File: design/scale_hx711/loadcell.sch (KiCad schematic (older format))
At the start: 12 parts

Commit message: Adds new footprints, and BoM.
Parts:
- J3: renamed from J?; footprint (none) -> Connector_JST:JST_EH_B4B-EH-A_1x04_P2.50mm_Vertical
- Q3: renamed from Q?; value BC560 -> BC857; footprint Package_TO_SOT_THT:TO-92_Inline -> Package_TO_SOT_SMD:SOT-23
- R6, R7, R8, R9: renamed from R?; footprint (none) -> Resistor_SMD:R_0603_1608Metric_Pad1.05x0.95mm_HandSolder
- U4: renamed from U?; footprint SO16 -> Package_SO:SOIC-16_3.9x9.9mm_P1.27mm
- gave numbers to parts that had none: 5
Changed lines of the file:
@@
 $EndDescr
 $Comp
-L sense:HX711 U?
+L sense:HX711 U4
 U 1 1 5E5FA3E6
 P 6100 3350
-F 0 "U?" H 6100 4410 45  0000 C CNN
+F 0 "U4" H 6100 4410 45  0000 C CNN
 F 1 "HX711" H 6100 4326 45  0000 C CNN
-F 2 "SO16" H 6100 4300 20  0001 C CNN
+F 2 "Package_SO:SOIC-16_3.9x9.9mm_P1.27mm" H 6100 4300 20  0001 C CNN
 F 3 "" H 6100 3350 50  0001 C CNN
 F 4 "IC-12445" H 6100 4231 60  0000 C CNN "Field4"
@@
 	6750 4050 6750 4100
 $Comp
-L sense:GND #PWR?
+L sense:GND #PWR0128
 U 1 1 5E64983B
 P 6750 4100
-F 0 "#PWR?" H 6750 3850 50  0001 C CNN
+F 0 "#PWR0128" H 6750 3850 50  0001 C CNN
 F 1 "GND" H 6750 3950 50  0000 C CNN
 F 2 "" H 6750 4100 60  0000 C CNN
@@
 $EndComp
 $Comp
-L sense:GND #PWR?
+L sense:GND #PWR0129
 U 1 1 5E649DC2
 P 6900 3950
-F 0 "#PWR?" H 6900 3700 50  0001 C CNN
+F 0 "#PWR0129" H 6900 3700 50  0001 C CNN
 F 1 "GND" H 6900 3800 50  0000 C CNN
 F 2 "" H 6900 3950 60  0000 C CNN
@@
 	6900 3050 6900 3150
 $Comp
-L sense:GND #PWR?
+L sense:GND #PWR0130
 U 1 1 5E65373D
 P 6900 3150
-F 0 "#PWR?" H 6900 2900 50  0001 C CNN
+F 0 "#PWR0130" H 6900 2900 50  0001 C CNN
 F 1 "GND" H 6900 3000 50  0000 C CNN
 F 2 "" H 6900 3150 60  0000 C CNN
@@
 	6800 2650 6800 2550
 $Comp
-L sense:VDD #PWR?
+L sense:VDD #PWR0131
 U 1 1 5E664FC5
 P 6800 2550
-F 0 "#PWR?" H 6800 2400 50  0001 C CNN
+F 0 "#PWR0131" H 6800 2400 50  0001 C CNN
 F 1 "VDD" H 6800 2700 50  0000 C CNN
 F 2 "" H 6800 2550 60  0000 C CNN
@@
 $EndComp
 $Comp
-L sense:C C?
+L sense:C C23
 U 1 1 5E6A1969
 P 4250 3850
-F 0 "C?" H 4300 3950 50  0000 L CNN
+F 0 "C23" H 4300 3950 50  0000 L CNN
 F 1 "0.1nF" H 4300 3750 50  0000 L CNN
 F 2 "sense_fp:C_0402_1005Metric" H 4288 3700 30  0001 C CNN
@@
 $EndComp
 $Comp
-L sense:GND #PWR?
+L sense:GND #PWR0132
 U 1 1 5E6A196F
 P 4250 4100
-F 0 "#PWR?" H 4250 3850 50  0001 C CNN
+F 0 "#PWR0132" H 4250 3850 50  0001 C CNN
 F 1 "GND" H 4250 3950 50  0000 C CNN
 F 2 "" H 4250 4100 60  0000 C CNN
@@
 	4250 3650 5550 3650
 $Comp
-L sense:R R?
+L sense:R R8
 U 1 1 5E6B26EF
 P 5050 3850
-F 0 "R?" V 4950 3850 50  0000 C CNN
+F 0 "R8" V 4950 3850 50  0000 C CNN
 F 1 "100" V 5050 3850 50  0000 C CNN
-F 2 "" V 4980 3850 50  0001 C CNN
+F 2 "Resistor_SMD:R_0603_1608Metric_Pad1.05x0.95mm_HandSolder" V 4980 3850 50  0001 C CNN
 F 3 "" H 5050 3850 50  0001 C CNN
 	1    5050 3850
@@
 	5200 3850 5300 3850
 $Comp
-L sense:R R?
+L sense:R R9
 U 1 1 5E6B963E
 P 5050 4250
-F 0 "R?" V 4950 4250 50  0000 C CNN
+F 0 "R9" V 4950 4250 50  0000 C CNN
 F 1 "100" V 5050 4250 50  0000 C CNN
-F 2 "" V 4980 4250 50  0001 C CNN
+F 2 "Resistor_SMD:R_0603_1608Metric_Pad1.05x0.95mm_HandSolder" V 4980 4250 50  0001 C CNN
 F 3 "" H 5050 4250 50  0001 C CNN
 	1    5050 4250
@@
 $EndComp
 $Comp
-L sense:C C?
+L sense:C C25
 U 1 1 5E6B9943
 P 5300 4050
-F 0 "C?" H 5150 4145 50  0000 L CNN
+F 0 "C25" H 5150 4145 50  0000 L CNN
 F 1 "0.1nF" H 5300 3950 50  0000 L CNN
 F 2 "sense_fp:C_0402_1005Metric" H 5338 3900 30  0001 C CNN
@@
 	4500 4250 4900 4250
 $Comp
-L sense:GND #PWR?
+L sense:GND #PWR0133
 U 1 1 5E6E6997
 P 5200 3450
-F 0 "#PWR?" H 5200 3200 50  0001 C CNN
+F 0 "#PWR0133" H 5200 3200 50  0001 C CNN
 F 1 "GND" H 5200 3300 50  0000 C CNN
 F 2 "" H 5200 3450 60  0000 C CNN
@@
 	5200 3450 5550 3450
 $Comp
-L sense:C C?
+L sense:C C26
 U 1 1 5E6F1C13
 P 7100 2200
-F 0 "C?" H 7125 2300 50  0000 L CNN
+F 0 "C26" H 7125 2300 50  0000 L CNN
 F 1 "0.1uF" H 7125 2100 50  0000 L CNN
 F 2 "sense_fp:C_1206_3216Metric" H 7138 2050 30  0001 C CNN
@@
 	7100 2400 7100 2350
 $Comp
-L sense:GND #PWR?
+L sense:GND #PWR0134
 U 1 1 5E6F1C1A
 P 7100 2400
-F 0 "#PWR?" H 7100 2150 50  0001 C CNN
+F 0 "#PWR0134" H 7100 2150 50  0001 C CNN
 F 1 "GND" H 7100 2250 50  0000 C CNN
 F 2 "" H 7100 2400 60  0000 C CNN
@@
 $EndComp
 $Comp
-L sense:VDD #PWR?
+L sense:VDD #PWR0135
 U 1 1 5E6F54A3
 P 7100 2000
-F 0 "#PWR?" H 7100 1850 50  0001 C CNN
+F 0 "#PWR0135" H 7100 1850 50  0001 C CNN
 F 1 "VDD" H 7100 2150 50  0000 C CNN
 F 2 "" H 7100 2000 60  0000 C CNN
@@
 	7100 2000 7100 2050
 $Comp
-L sense:R R?
+L sense:R R6
 U 1 1 5E7095DC
 P 4200 3250
-F 0 "R?" V 4100 3250 50  0000 C CNN
+F 0 "R6" V 4100 3250 50  0000 C CNN
 F 1 "100" V 4200 3250 50  0000 C CNN
-F 2 "" V 4130 3250 50  0001 C CNN
+F 2 "Resistor_SMD:R_0603_1608Metric_Pad1.05x0.95mm_HandSolder" V 4130 3250 50  0001 C CNN
 F 3 "" H 4200 3250 50  0001 C CNN
 	1    4200 3250
@@
 $EndComp
 $Comp
-L sense:GND #PWR?
+L sense:GND #PWR0136
 U 1 1 5E709A9D
 P 4000 3350
-F 0 "#PWR?" H 4000 3100 50  0001 C CNN
+F 0 "#PWR0136" H 4000 3100 50  0001 C CNN
 F 1 "GND" H 4000 3200 50  0000 C CNN
 F 2 "" H 4000 3350 60  0000 C CNN
@@
 	4350 3250 4400 3250
 $Comp
-L sense:R R?
+L sense:R R7
 U 1 1 5E72BB5A
 P 4600 3050
-F 0 "R?" V 4500 3050 50  0000 C CNN
+F 0 "R7" V 4500 3050 50  0000 C CNN
 F 1 "100" V 4600 3050 50  0000 C CNN
-F 2 "" V 4530 3050 50  0001 C CNN
+F 2 "Resistor_SMD:R_0603_1608Metric_Pad1.05x0.95mm_HandSolder" V 4530 3050 50  0001 C CNN
 F 3 "" H 4600 3050 50  0001 C CNN
 	1    4600 3050
@@
 	5250 2700 5300 2700
 $Comp
-L Transistor_BJT:BC560 Q?
+L Transistor_BJT:BC560 Q3
 U 1 1 5E7513ED
 P 5050 2700
-F 0 "Q?" H 4900 2600 50  0000 L CNN
-F 1 "BC560" H 4850 2900 50  0000 L CNN
-F 2 "Package_TO_SOT_THT:TO-92_Inline" H 5250 2625 50  0001 L CIN
+F 0 "Q3" H 4900 2600 50  0000 L CNN
+F 1 "BC857" H 4850 2900 50  0000 L CNN
+F 2 "Package_TO_SOT_SMD:SOT-23" H 5250 2625 50  0001 L CIN
 F 3 "http://www.fairchildsemi.com/ds/BC/BC557.pdf" H 5050 2700 50  0001 L CNN
 	1    5050 2700
@@
 	4950 2450 5500 2450
 $Comp
-L sense:C C?
+L sense:C C24
 U 1 1 5E78810B
 P 4550 2450
-F 0 "C?" H 4575 2550 50  0000 L CNN
+F 0 "C24" H 4575 2550 50  0000 L CNN
 F 1 "10uF" H 4350 2350 50  0000 L CNN
 F 2 "sense_fp:C_1206_3216Metric" H 4588 2300 30  0001 C CNN
@@
 	4550 2150 4550 2300
 $Comp
-L sense:GND #PWR?
+L sense:GND #PWR0137
 U 1 1 5E788114
 P 4550 2650
-F 0 "#PWR?" H 4550 2400 50  0001 C CNN
+F 0 "#PWR0137" H 4550 2400 50  0001 C CNN
 F 1 "GND" H 4550 2500 50  0000 C CNN
 F 2 "" H 4550 2650 60  0000 C CNN
@@
 VBAT
 $Comp
-L sense:C C?
+L sense:C C22
 U 1 1 5E7AC1CA
 P 4100 2450
-F 0 "C?" H 4125 2550 50  0000 L CNN
+F 0 "C22" H 4125 2550 50  0000 L CNN
 F 1 "10uF" H 3900 2350 50  0000 L CNN
 F 2 "sense_fp:C_1206_3216Metric" H 4138 2300 30  0001 C CNN
@@
 	4100 2150 4100 2300
 $Comp
-L sense:GND #PWR?
+L sense:GND #PWR0138
 U 1 1 5E7AC1D3
 P 4100 2650
-F 0 "#PWR?" H 4100 2400 50  0001 C CNN
+F 0 "#PWR0138" H 4100 2400 50  0001 C CNN
 F 1 "GND" H 4100 2500 50  0000 C CNN
 F 2 "" H 4100 2650 60  0000 C CNN
@@
 NoConn ~ 6650 3250
 $Comp
-L sense:Conn_01x04 J?
+L sense:Conn_01x04 J3
 U 1 1 5E7BE76B
 P 2000 3200
-F 0 "J?" H 1918 2775 50  0000 C CNN
+F 0 "J3" H 1918 2775 50  0000 C CNN
 F 1 "Load cell" H 1918 2866 50  0000 C CNN
-F 2 "" H 2000 3200 50  0001 C CNN
+F 2 "Connector_JST:JST_EH_B4B-EH-A_1x04_P2.50mm_Vertical" H 2000 3200 50  0001 C CNN
 F 3 "" H 2000 3200 50  0001 C CNN
 	1    2000 3200
@@
 	2850 3100 2850 3200
 $Comp
-L sense:GND #PWR?
+L sense:GND #PWR0139
 U 1 1 5E7D7679
 P 2850 3200
-F 0 "#PWR?" H 2850 2950 50  0001 C CNN
+F 0 "#PWR0139" H 2850 2950 50  0001 C CNN
 F 1 "GND" H 2850 3050 50  0000 C CNN
 F 2 "" H 2850 3200 60  0000 C CNN

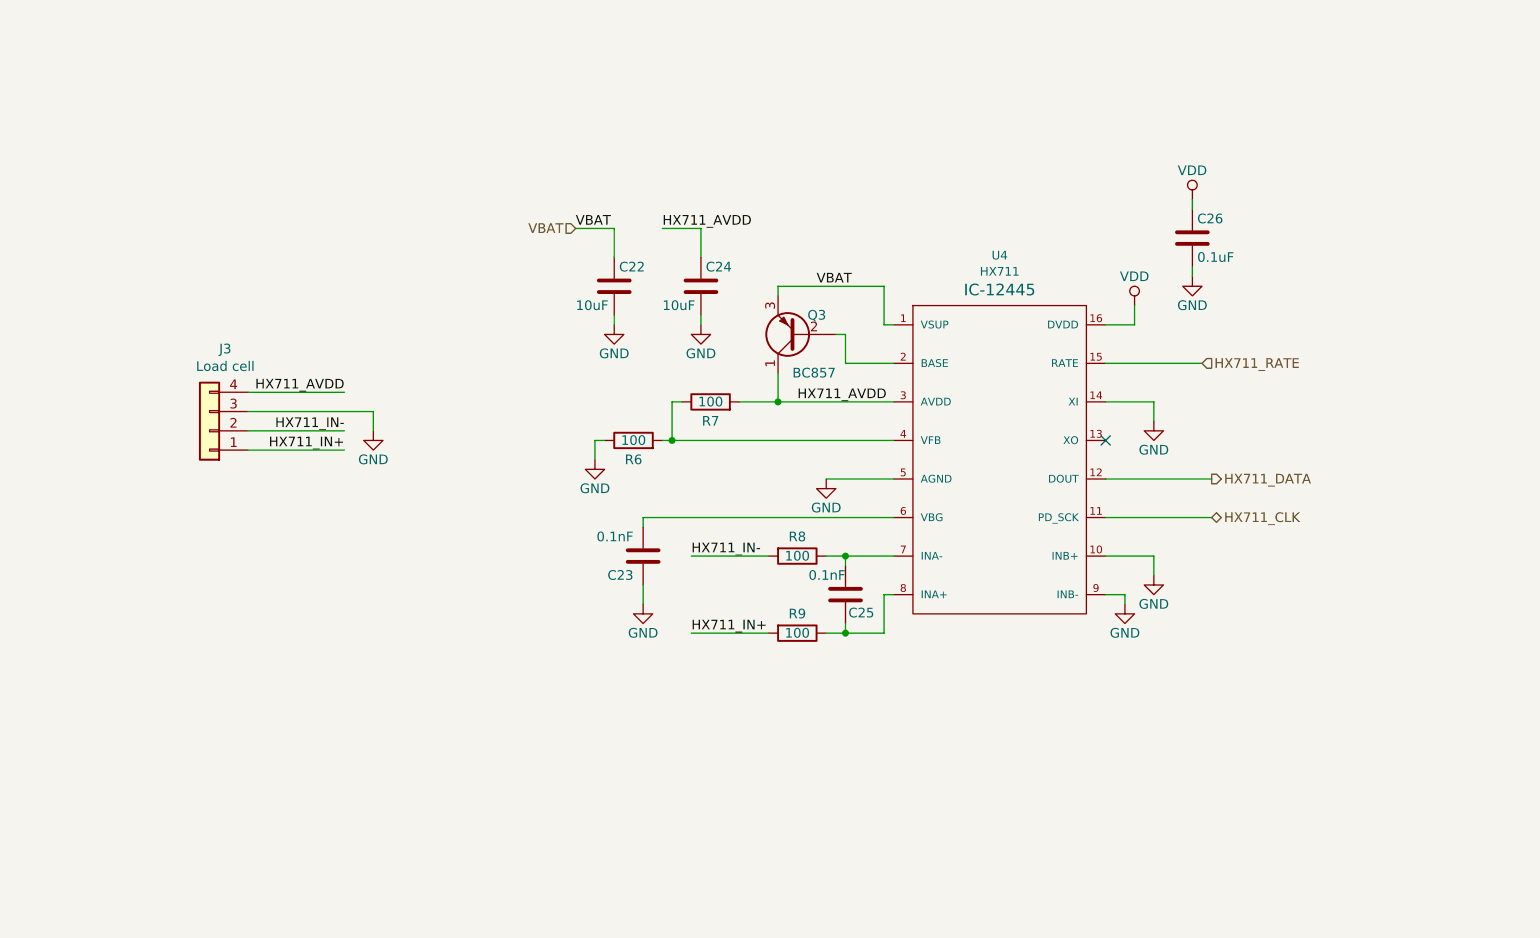
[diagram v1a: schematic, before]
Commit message: Schematics, BoM updated. New project added - scale_ltc6915
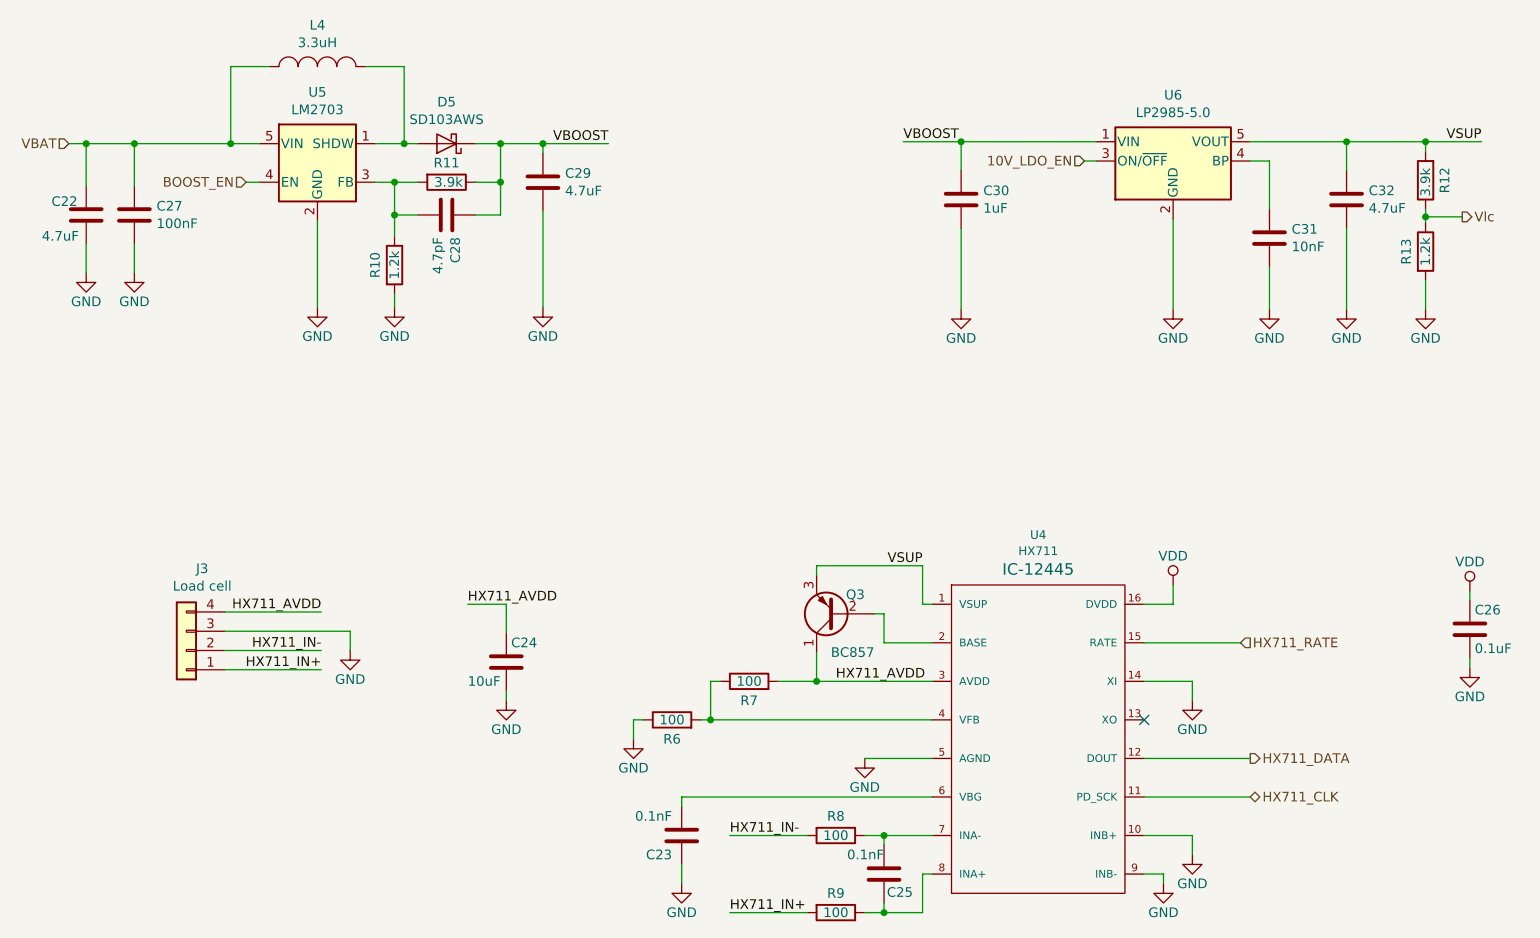
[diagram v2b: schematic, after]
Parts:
- removed C22: 10uF, sense_fp:C_1206_3216Metric, symbol sense:C
- added C22, C29, C32: 4.7uF, Capacitor_SMD:C_0603_1608Metric_Pad1.05x0.95mm_HandSolder, symbol Device:C
- added C27: 100nF, Capacitor_SMD:C_0603_1608Metric_Pad1.05x0.95mm_HandSolder, symbol Device:C
- added C28: 4.7pF, Capacitor_SMD:C_0603_1608Metric_Pad1.05x0.95mm_HandSolder, symbol Device:C
- added C30: 1uF, Capacitor_SMD:C_0603_1608Metric_Pad1.05x0.95mm_HandSolder, symbol Device:C
- added C31: 10nF, Capacitor_SMD:C_0603_1608Metric_Pad1.05x0.95mm_HandSolder, symbol Device:C
- added D5: SD103AWS, Diode_SMD:D_SOD-323_HandSoldering, symbol Device:D_Schottky
- added L4: 3.3uH, Footprint_nrf_scale:L_3.5x3.0mm_CD30D22, symbol sense:INDUCTOR_SMALL
- added R10, R13: 1.2k, Resistor_SMD:R_0603_1608Metric_Pad1.05x0.95mm_HandSolder, symbol sense:R
- added R11, R12: 3.9k, Resistor_SMD:R_0603_1608Metric_Pad1.05x0.95mm_HandSolder, symbol sense:R
- added U5: LM2703, Package_TO_SOT_SMD:SOT-23-5, symbol sense:LM2703
- added U6: LP2985-5.0, Package_TO_SOT_SMD:SOT-23-5, symbol Regulator_Linear:LP2985-5.0
- J3: footprint Connector_JST:JST_EH_B4B-EH-A_1x04_P2.50mm_Vertical -> Connector_JST:JST_PH_B4B-PH-K_1x04_P2.00mm_Vertical
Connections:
- net GND: now also C22.2, C27.2, C29.2, C30.2, C31.2, C32.2, R10.2, R13.2, U5.2 (GND), U6.2 (GND)
- net VBAT: now also C22.1, C27.1, L4.1, U5.5 (VIN); no longer Q3.3 (E), U4.1 (VSUP)
- new net: C31.1, U6.4 (BP)
- new net: D5.2 (A), L4.2, U5.1 (SHDW)
- new net: C28.2, R10.1, R11.2, U5.3 (FB)
- new net 10V_LDO_EN: U6.3 (ON/~OFF~)
- new net BOOST_EN: U5.4 (EN)
- new net VBOOST: C28.1, C29.1, C30.1, D5.1 (K), R11.1, U6.1 (VIN)
- new net VSUP: C32.1, Q3.3 (E), R12.2, U4.1 (VSUP), U6.5 (VOUT)
- new net Vlc: R12.1, R13.1
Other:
- moved on the sheet: C23, C24, C25, C26, J3, Q3, R6, R7, R8, R9, U4

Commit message: BOMs, schematics updated, scale_ltc6915 PCB Design complete.
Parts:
- R6: value 100 -> 4.7k
- R7: value 100 -> 24k
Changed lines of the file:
@@
 P 4400 4700
 F 0 "R6" V 4300 4700 50  0000 C CNN
-F 1 "100" V 4400 4700 50  0000 C CNN
+F 1 "4.7k" V 4400 4700 50  0000 C CNN
 F 2 "Resistor_SMD:R_0603_1608Metric_Pad1.05x0.95mm_HandSolder" V 4330 4700 50  0001 C CNN
 F 3 "" H 4400 4700 50  0001 C CNN
@@
 P 4800 4500
 F 0 "R7" V 4700 4500 50  0000 C CNN
-F 1 "100" V 4800 4500 50  0000 C CNN
+F 1 "24k" V 4800 4500 50  0000 C CNN
 F 2 "Resistor_SMD:R_0603_1608Metric_Pad1.05x0.95mm_HandSolder" V 4730 4500 50  0001 C CNN
 F 3 "" H 4800 4500 50  0001 C CNN
